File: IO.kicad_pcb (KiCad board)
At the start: 2 copper layers, 95 x 72 mm, 23 parts, among them CN1 DC5V, CN2 XH Nu1.1_UART2_Control, CN3 Alt TEST SW

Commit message: Logo changed, Pwr LED moved
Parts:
- added G***: LOGO, logos:revio, F.Cu at (85.1, 105.4)
- moved PWR_LED1 3.70 mm to (74.3, 75.6)
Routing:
- net Net-(PWR_LED1-Pad2): track 3.81 -> 8.15 mm
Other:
- board text removed: "REVIO r2"

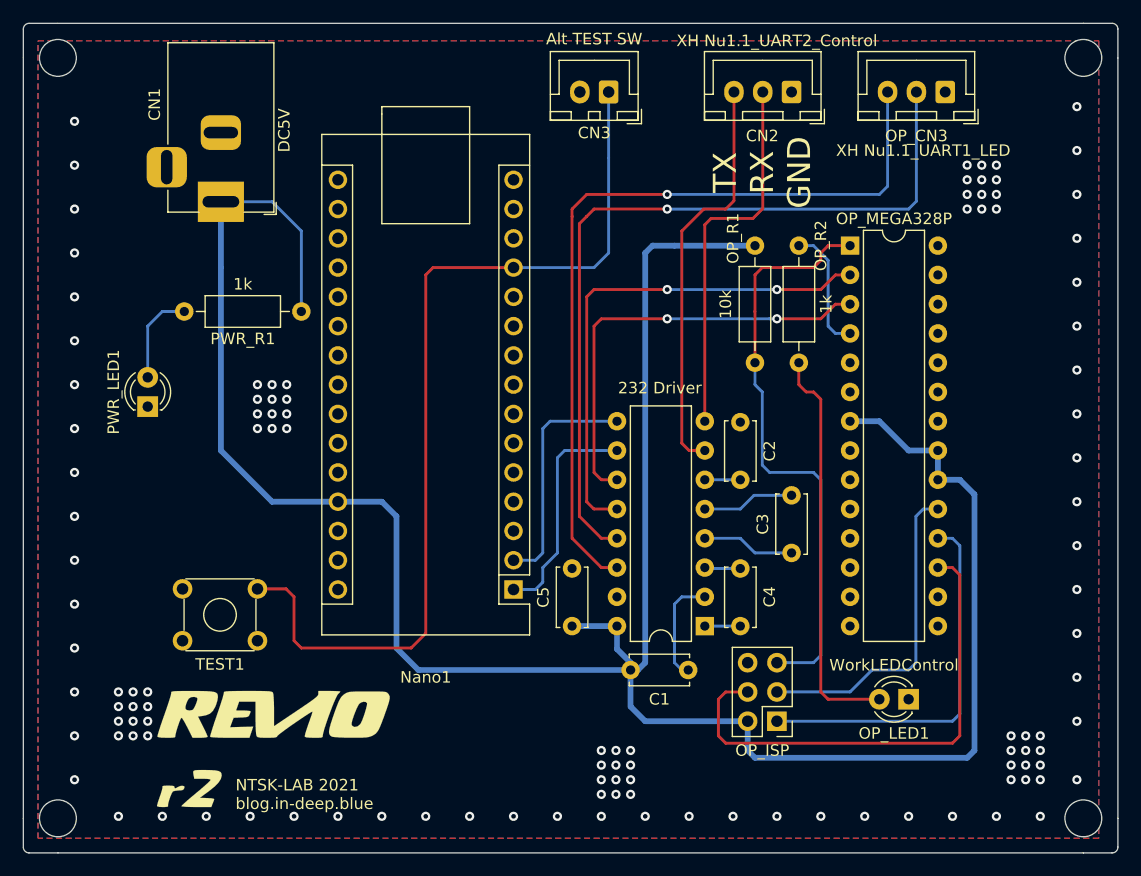
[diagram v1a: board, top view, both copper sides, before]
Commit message: add xad22, led interrupt circuit
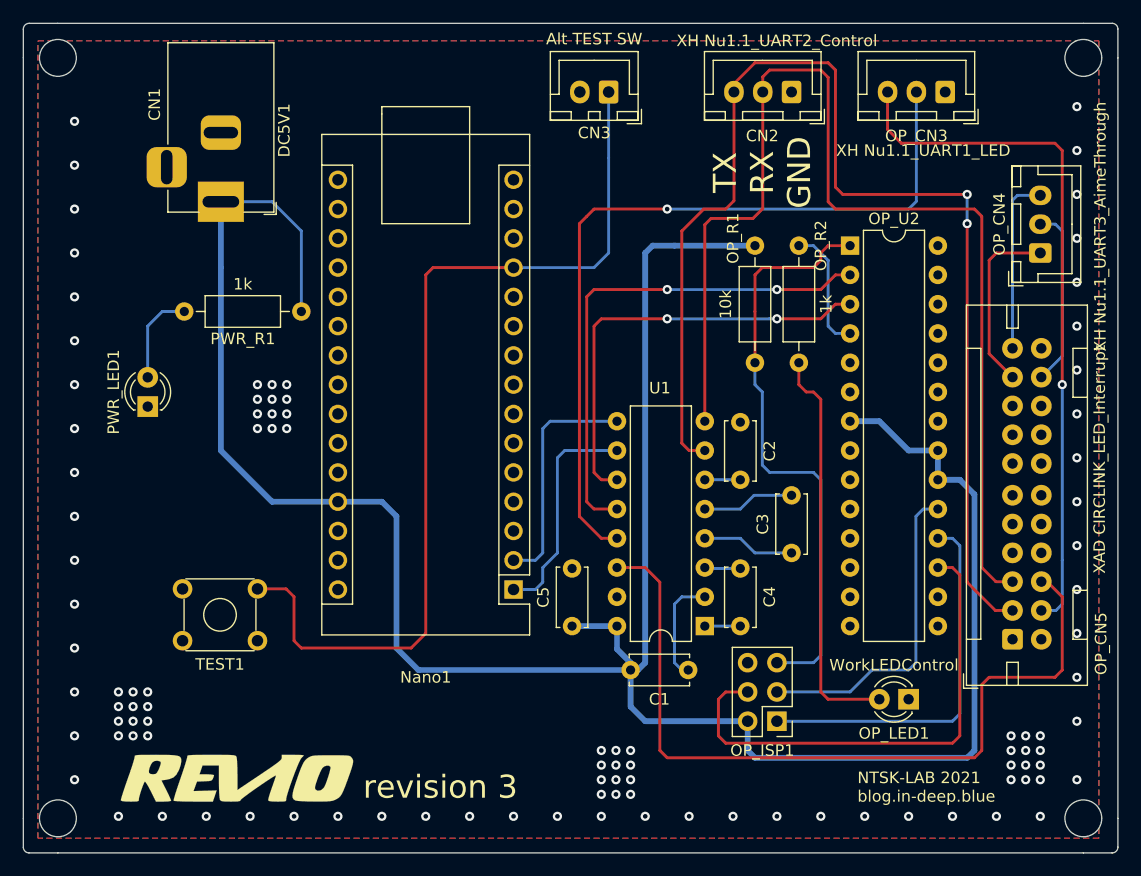
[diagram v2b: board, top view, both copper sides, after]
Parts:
- removed G***: LOGO, logos:revio
- removed REF** (x4): MountingHole_3.2mm_M3, MountingHole:MountingHole_3.2mm_M3
- added H1: MountingHole, MountingHole:MountingHole_3.2mm_M3, F.Cu at (66.5, 45.3)
- added H2: MountingHole, MountingHole:MountingHole_3.2mm_M3, F.Cu at (155.5, 45.3)
- added H3: MountingHole, MountingHole:MountingHole_3.2mm_M3, F.Cu at (66.5, 111.3)
- added H4: MountingHole, MountingHole:MountingHole_3.2mm_M3, F.Cu at (155.5, 111.3)
- added Logo1: Logo, logos:revio, F.Cu at (81.9, 108.0)
- added OP_CN4: XH Nu1.1_UART3_AimeThrough, Connector_JST:JST_XH_B3B-XH-A_1x03_P2.50mm_Vertical, F.Cu at (151.8, 62.2)
- added OP_CN5: XAD CIRCLINK_LED_Interrupt, footprint:JST_XAD_B22B-XADSS-N_2x11_P2.50mm_Vertical, F.Cu at (149.4, 95.8)
- CN1: value DC5V -> DC5V1
- U1: renamed from 232 Driver
- renumbered OP_ISP to OP_ISP1, OP_MEGA328P to OP_U2
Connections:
- TEST1 pad 1: (no net) -> Net-(CN3-Pad1)
- TEST1 pad 3: Net-(CN3-Pad1) -> (no net)
- TEST1 pad 4: GND -> (no net)
- U1 pad 14: Net-(OP_CN3-Pad3) -> Net-(OP_CN5-Pad6)
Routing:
- net Net-(CN2-Pad3): track 35.7 -> 106.7 mm, vias 0 -> 2
- net Net-(OP_CN5-Pad6): track 0.00 -> 69.3 mm
- net Net-(CN2-Pad2): track 32.8 -> 98.6 mm
- net Net-(OP_CN4-Pad1): track 0.00 -> 15.7 mm
- net Net-(OP_CN4-Pad2): track 0.00 -> 15.6 mm
- net Net-(OP_CN4-Pad3): track 0.00 -> 15.4 mm
- net Net-(OP_CN3-Pad3): track 69.9 -> 60.6 mm
- net GND: vias 114 -> 102
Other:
- board text added: "revision 3"

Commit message: add arduino replace option
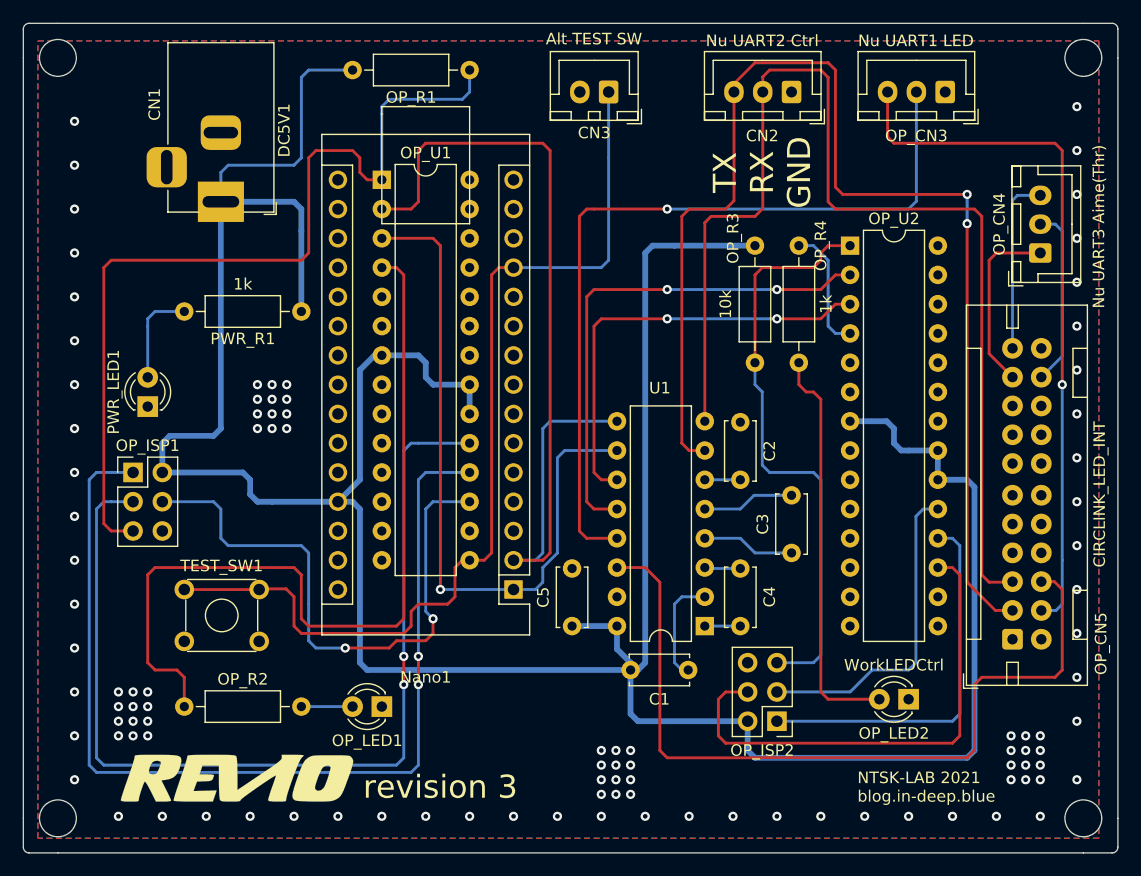
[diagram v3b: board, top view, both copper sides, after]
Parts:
- removed TEST1: SW_Push, Button_Switch_THT:SW_TH_Tactile_Omron_B3F-10xx
- added OP_ISP1: Conn_01x06, Connector_PinHeader_2.54mm:PinHeader_2x03_P2.54mm_Vertical, F.Cu at (73.0, 81.3)
- added OP_LED1: WorkCtrl, LED_THT:LED_D3.0mm, F.Cu at (94.6, 101.6)
- added OP_R1: 10k, Resistor_THT:R_Axial_DIN0207_L6.3mm_D2.5mm_P10.16mm_Horizontal, F.Cu at (102.2, 46.4)
- added OP_R2: 1k, Resistor_THT:R_Axial_DIN0207_L6.3mm_D2.5mm_P10.16mm_Horizontal, F.Cu at (77.5, 101.6)
- added OP_U1: ATmega328P-PU, Package_DIP:DIP-28_W7.62mm, F.Cu at (94.6, 55.9)
- added TEST_SW1: SW_MEC_5E, Button_Switch_THT:SW_TH_Tactile_Omron_B3F-10xx, F.Cu at (77.5, 91.4)
- CN2: value XH Nu1.1_UART2_Control -> Nu UART2 Ctrl
- OP_CN3: value XH Nu1.1_UART1_LED -> Nu UART1 LED
- OP_CN4: value XH Nu1.1_UART3_AimeThrough -> Nu UART3 Aime(Thr)
- OP_CN5: value XAD CIRCLINK_LED_Interrupt -> CIRCLINK_LED_INT
- OP_LED2: renamed from OP_LED1; value WorkLEDControl -> WorkLEDCtrl
- renumbered OP_ISP1 to OP_ISP2, OP_R1 to OP_R3, OP_R2 to OP_R4
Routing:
- net Net-(OP_ISP1-Pad1): track 0.00 -> 87.4 mm, vias 0 -> 2
- net Net-(OP_ISP1-Pad3): track 0.00 -> 84.9 mm, vias 0 -> 2
- net Net-(OP_ISP1-Pad5): track 0.00 -> 76.4 mm
- net Net-(OP_R2-Pad1): track 0.00 -> 73.0 mm
- net +5V: track 216.0 -> 279.4 mm
- net Net-(Nano1-Pad2): track 20.3 -> 78.5 mm
- net Net-(OP_ISP1-Pad4): track 0.00 -> 50.4 mm, vias 0 -> 2
- net Net-(Nano1-Pad1): track 19.6 -> 61.1 mm, vias 0 -> 1
- net Net-(OP_LED1-Pad2): track 0.00 -> 4.45 mm
- net Net-(CN3-Pad1): track 81.2 -> 84.3 mm
- net Net-(OP_CN3-Pad2): track 69.0 -> 70.1 mm
- net Net-(CN2-Pad3): track 106.7 -> 107.5 mm
- net Net-(CN2-Pad2): track 98.6 -> 99.1 mm
